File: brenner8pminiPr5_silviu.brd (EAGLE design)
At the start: 82.5 x 43 mm, 39 parts, among them IC1 PIC18F2550SP, Q1 20 MHz, Q2 BC338-25, Q3 BC338-25, Q4 BC328-25, Q5 BC328-25, Q6 BF959, X2 USB-B-H

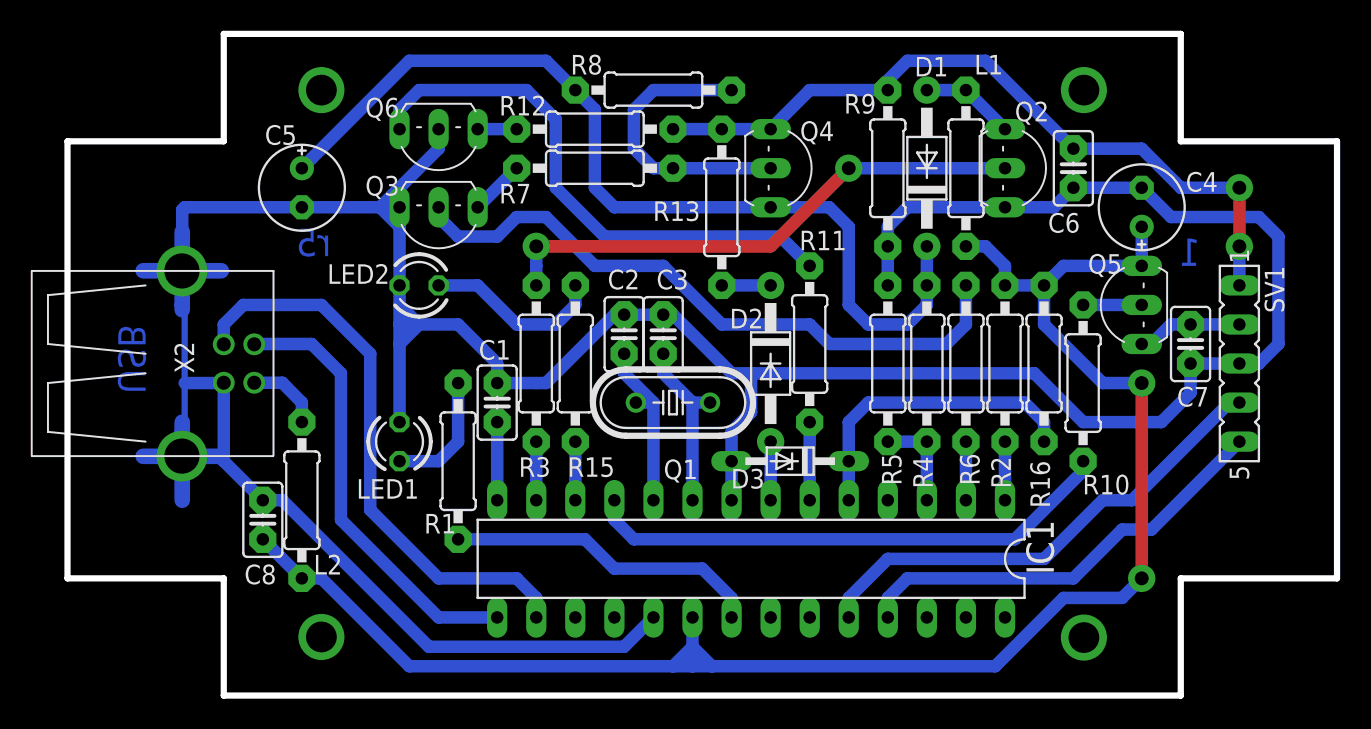
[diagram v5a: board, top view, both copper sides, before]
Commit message: Fixed D2-D3 overlap
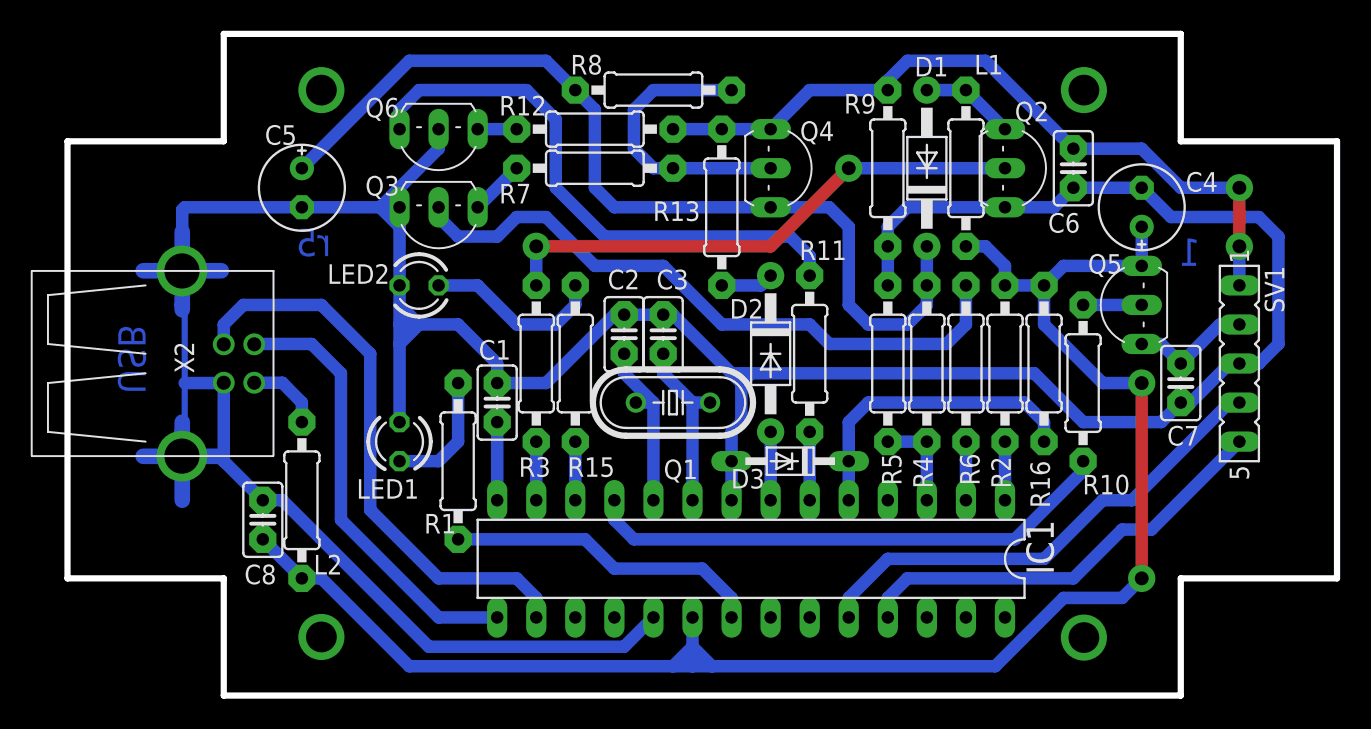
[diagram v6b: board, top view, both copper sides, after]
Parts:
- moved C7 2.62 mm to (72.4, 19.1)
- moved R11 0.64 mm to (48.3, 21.0)
- moved D2 0.63 mm to (45.7, 21.0)
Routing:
- net VSS: track 232.3 -> 231.0 mm
- net N$17: track 6.88 -> 7.93 mm
- net N$19: track 35.8 -> 36.8 mm
- net N$20: track 5.08 -> 4.45 mm
- net N$25: track 3.81 -> 4.45 mm
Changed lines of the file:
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@@
 <attribute name="VALUE" x="66.675" y="16.7894" size="1.27" layer="27" ratio="10" rot="R90"/>
 </element>
-<element name="C7" library="rcl" package="C025-025X050" value="100nF" x="73.025" y="21.59" smashed="yes" rot="R270">
-<attribute name="NAME" x="72.136" y="17.526" size="1.27" layer="25" ratio="10"/>
-<attribute name="VALUE" x="72.771" y="18.669" size="1.27" layer="27" ratio="10" rot="R270"/>
-</element>
-<element name="R11" library="rcl" package="0207/10" value="10k" x="48.26" y="21.59" smashed="yes" rot="R90">
-<attribute name="NAME" x="50.673" y="28.956" size="1.27" layer="25" ratio="10" rot="R180"/>
-<attribute name="VALUE" x="48.895" y="19.3294" size="1.27" layer="27" ratio="10" rot="R90"/>
+<element name="C7" library="rcl" package="C025-025X050" value="100nF" x="72.39" y="19.05" smashed="yes" rot="R270">
+<attribute name="NAME" x="71.501" y="14.986" size="1.27" layer="25" ratio="10"/>
+<attribute name="VALUE" x="72.136" y="16.129" size="1.27" layer="27" ratio="10" rot="R270"/>
+</element>
+<element name="R11" library="rcl" package="0207/10" value="10k" x="48.26" y="20.955" smashed="yes" rot="R90">
+<attribute name="NAME" x="50.673" y="28.321" size="1.27" layer="25" ratio="10" rot="R180"/>
+<attribute name="VALUE" x="48.895" y="18.6944" size="1.27" layer="27" ratio="10" rot="R90"/>
 </element>
 <element name="R12" library="rcl" package="0207/10" value="100" x="34.29" y="35.56" smashed="yes">
@@
 <attribute name="VALUE" x="43.18" y="29.4894" size="1.27" layer="27" ratio="10" rot="R90"/>
 </element>
-<element name="D2" library="diode" package="DO41-10" value="BAT43" x="45.72" y="20.32" smashed="yes" rot="R270">
-<attribute name="NAME" x="43.053" y="22.606" size="1.27" layer="25" ratio="10"/>
-<attribute name="VALUE" x="42.291" y="24.892" size="1.27" layer="27" ratio="10" rot="R270"/>
+<element name="D2" library="diode" package="DO41-10" value="BAT43" x="45.72" y="20.955" smashed="yes" rot="R270">
+<attribute name="NAME" x="43.053" y="23.241" size="1.27" layer="25" ratio="10"/>
+<attribute name="VALUE" x="42.291" y="25.527" size="1.27" layer="27" ratio="10" rot="R270"/>
 </element>
 <element name="Q6" library="sprut" package="TO92-BEC" value="BF959" x="24.13" y="35.56" smashed="yes" rot="R180">
@@
 <wire x1="30.48" y1="27.94" x2="45.72" y2="27.94" width="0.8128" layer="1"/>
 <wire x1="45.72" y1="27.94" x2="50.8" y2="33.02" width="0.8128" layer="1"/>
-<wire x1="30.48" y1="26.67" x2="30.48" y2="27.94" width="0.8128" layer="16"/>
-<wire x1="30.48" y1="26.67" x2="30.48" y2="25.4" width="0.8128" layer="16"/>
+<wire x1="30.48" y1="27.94" x2="30.48" y2="25.4" width="0.8128" layer="16"/>
 <via x="50.8" y="33.02" extent="1-16" drill="0.9" diameter="1.778"/>
 <via x="30.48" y="27.94" extent="1-16" drill="0.9" diameter="1.778"/>
@@
 <wire x1="34.29" y1="36.83" x2="34.29" y2="31.75" width="0.8128" layer="16"/>
 <wire x1="34.29" y1="31.75" x2="35.56" y2="30.48" width="0.8128" layer="16"/>
-<wire x1="15.24" y1="33.02" x2="15.875" y2="33.655" width="0.8128" layer="16"/>
-<wire x1="15.875" y1="33.655" x2="22.225" y2="40.005" width="0.8128" layer="16"/>
+<wire x1="15.24" y1="33.02" x2="22.225" y2="40.005" width="0.8128" layer="16"/>
 <wire x1="22.225" y1="40.005" x2="31.115" y2="40.005" width="0.8128" layer="16"/>
 <wire x1="31.115" y1="40.005" x2="33.02" y2="38.1" width="0.8128" layer="16"/>
@@
 <contactref element="R1" pad="1"/>
 <contactref element="IC1" pad="21"/>
-<wire x1="25.4" y1="8.89" x2="26.035" y2="8.89" width="0.8128" layer="16"/>
-<wire x1="26.035" y1="8.89" x2="33.655" y2="8.89" width="0.8128" layer="16"/>
+<wire x1="25.4" y1="8.89" x2="33.655" y2="8.89" width="0.8128" layer="16"/>
 <wire x1="33.655" y1="8.89" x2="35.56" y2="6.985" width="0.8128" layer="16"/>
 <wire x1="35.56" y1="6.985" x2="41.275" y2="6.985" width="0.8128" layer="16"/>
@@
 <contactref element="Q5" pad="C"/>
 <contactref element="C7" pad="1"/>
-<wire x1="69.85" y1="21.59" x2="70.485" y2="21.59" width="0.8128" layer="16"/>
-<wire x1="70.485" y1="21.59" x2="71.755" y2="22.86" width="0.8128" layer="16"/>
-<wire x1="71.755" y1="22.86" x2="73.025" y2="22.86" width="0.8128" layer="16"/>
-<wire x1="73.025" y1="22.86" x2="76.2" y2="22.86" width="0.8128" layer="16"/>
+<wire x1="69.85" y1="21.59" x2="71.12" y2="21.59" width="0.8128" layer="16"/>
+<wire x1="71.12" y1="21.59" x2="72.39" y2="20.32" width="0.8128" layer="16"/>
+<wire x1="72.39" y1="20.32" x2="74.93" y2="22.86" width="0.8128" layer="16"/>
+<wire x1="74.93" y1="22.86" x2="76.2" y2="22.86" width="0.8128" layer="16"/>
 </signal>
 <signal name="N$19">
 <contactref element="R11" pad="2"/>
 <contactref element="Q6" pad="B"/>
-<wire x1="46.355" y1="28.575" x2="48.26" y2="26.67" width="0.8128" layer="16"/>
-<wire x1="34.925" y1="28.575" x2="46.355" y2="28.575" width="0.8128" layer="16"/>
+<wire x1="46.99" y1="28.575" x2="48.26" y2="27.305" width="0.8128" layer="16"/>
+<wire x1="48.26" y1="27.305" x2="48.26" y2="26.035" width="0.8128" layer="16"/>
+<wire x1="34.925" y1="28.575" x2="46.99" y2="28.575" width="0.8128" layer="16"/>
 <wire x1="31.75" y1="31.75" x2="34.925" y2="28.575" width="0.8128" layer="16"/>
 <wire x1="31.75" y1="36.195" x2="31.75" y2="31.75" width="0.8128" layer="16"/>
@@
 <contactref element="R11" pad="1"/>
 <contactref element="IC1" pad="6"/>
-<wire x1="48.26" y1="11.43" x2="48.26" y2="16.51" width="0.8128" layer="16"/>
+<wire x1="48.26" y1="11.43" x2="48.26" y2="15.875" width="0.8128" layer="16"/>
 </signal>
 <signal name="N$22">
@@
 <contactref element="IC1" pad="7"/>
 <contactref element="D2" pad="A"/>
-<wire x1="45.72" y1="11.43" x2="45.72" y2="15.24" width="0.8128" layer="16"/>
+<wire x1="45.72" y1="11.43" x2="45.72" y2="15.875" width="0.8128" layer="16"/>
 </signal>
 <signal name="N$26">
 <contactref element="D2" pad="C"/>
 <contactref element="R13" pad="1"/>
-<wire x1="42.545" y1="25.4" x2="45.72" y2="25.4" width="0.8128" layer="16"/>
+<wire x1="42.545" y1="25.4" x2="45.085" y2="25.4" width="0.8128" layer="16"/>
+<wire x1="45.085" y1="25.4" x2="45.72" y2="26.035" width="0.8128" layer="16"/>
 </signal>
 <signal name="VDD">
@@
 <wire x1="66.04" y1="16.51" x2="71.12" y2="16.51" width="0.8128" layer="16"/>
 <wire x1="43.18" y1="13.97" x2="43.18" y2="11.43" width="0.8128" layer="16"/>
-<wire x1="44.45" y1="17.145" x2="43.18" y2="15.875" width="0.8128" layer="16"/>
+<wire x1="43.815" y1="16.51" x2="43.18" y2="15.875" width="0.8128" layer="16"/>
 <wire x1="43.18" y1="15.875" x2="43.18" y2="13.97" width="0.8128" layer="16"/>
 <wire x1="77.47" y1="29.845" x2="71.755" y2="29.845" width="0.8128" layer="16"/>
-<wire x1="27.94" y1="19.05" x2="30.48" y2="19.05" width="0.8128" layer="16"/>
-<wire x1="30.48" y1="19.05" x2="31.115" y2="19.05" width="0.8128" layer="16"/>
+<wire x1="27.94" y1="19.05" x2="31.115" y2="19.05" width="0.8128" layer="16"/>
 <wire x1="10.16" y1="19.05" x2="10.16" y2="19.07" width="0.8128" layer="16"/>
 <wire x1="10.16" y1="13.97" x2="12.7" y2="11.43" width="0.8128" layer="16"/>
@@
 <wire x1="7.4612" y1="11.43" x2="7.4612" y2="15.875" width="1.016" layer="16"/>
 <wire x1="7.4612" y1="15.875" x2="7.4612" y2="16.51" width="1.016" layer="16"/>
-<wire x1="43.18" y1="19.685" x2="44.45" y2="19.685" width="0.8128" layer="16"/>
+<wire x1="43.18" y1="19.685" x2="43.815" y2="19.685" width="0.8128" layer="16"/>
+<wire x1="43.815" y1="19.685" x2="44.45" y2="19.685" width="0.8128" layer="16"/>
 <wire x1="44.45" y1="19.685" x2="62.865" y2="19.685" width="0.8128" layer="16"/>
 <wire x1="36.195" y1="1.905" x2="38.1" y2="3.81" width="0.8128" layer="16"/>
@@
 <wire x1="21.59" y1="22.86" x2="22.86" y2="22.86" width="0.8128" layer="16"/>
 <wire x1="22.86" y1="22.86" x2="25.4" y2="22.86" width="0.8128" layer="16"/>
-<wire x1="71.12" y1="16.51" x2="73.025" y2="18.415" width="0.8128" layer="16"/>
-<wire x1="73.025" y1="18.415" x2="73.025" y2="20.32" width="0.8128" layer="16"/>
-<wire x1="73.025" y1="20.32" x2="76.2" y2="20.32" width="0.8128" layer="16"/>
+<wire x1="71.12" y1="16.51" x2="72.39" y2="17.78" width="0.8128" layer="16"/>
 <wire x1="36.195" y1="23.495" x2="38.735" y2="23.495" width="0.8128" layer="16"/>
 <wire x1="35.56" y1="23.495" x2="36.195" y2="23.495" width="0.8128" layer="16"/>
@@
 <wire x1="21.59" y1="30.48" x2="21.59" y2="31.75" width="0.8128" layer="16"/>
 <wire x1="24.13" y1="34.29" x2="24.13" y2="35.56" width="0.8128" layer="16"/>
-<wire x1="44.45" y1="17.145" x2="44.45" y2="19.685" width="0.8128" layer="16"/>
+<wire x1="43.815" y1="16.51" x2="43.815" y2="19.05" width="0.8128" layer="16"/>
+<wire x1="43.815" y1="19.05" x2="43.815" y2="19.685" width="0.8128" layer="16"/>
 <wire x1="21.59" y1="21.59" x2="22.86" y2="22.86" width="0.8128" layer="16"/>
 <wire x1="22.86" y1="22.86" x2="21.59" y2="24.13" width="0.8128" layer="16"/>
-<wire x1="20.32" y1="30.48" x2="21.59" y2="31.75" width="0.8128" layer="16"/>
 <wire x1="21.59" y1="31.75" x2="20.32" y2="30.48" width="0.8128" layer="16"/>
 <wire x1="21.59" y1="29.21" x2="20.32" y2="30.48" width="0.8128" layer="16"/>
+<wire x1="72.39" y1="17.78" x2="73.025" y2="17.78" width="0.8128" layer="16"/>
+<wire x1="73.025" y1="17.78" x2="75.565" y2="20.32" width="0.8128" layer="16"/>
+<wire x1="75.565" y1="20.32" x2="76.2" y2="20.32" width="0.8128" layer="16"/>
+<wire x1="43.18" y1="19.685" x2="43.815" y2="19.05" width="0.8128" layer="16"/>
+<wire x1="43.815" y1="19.05" x2="44.45" y2="19.685" width="0.8128" layer="16"/>
 </signal>
 <signal name="N$29">

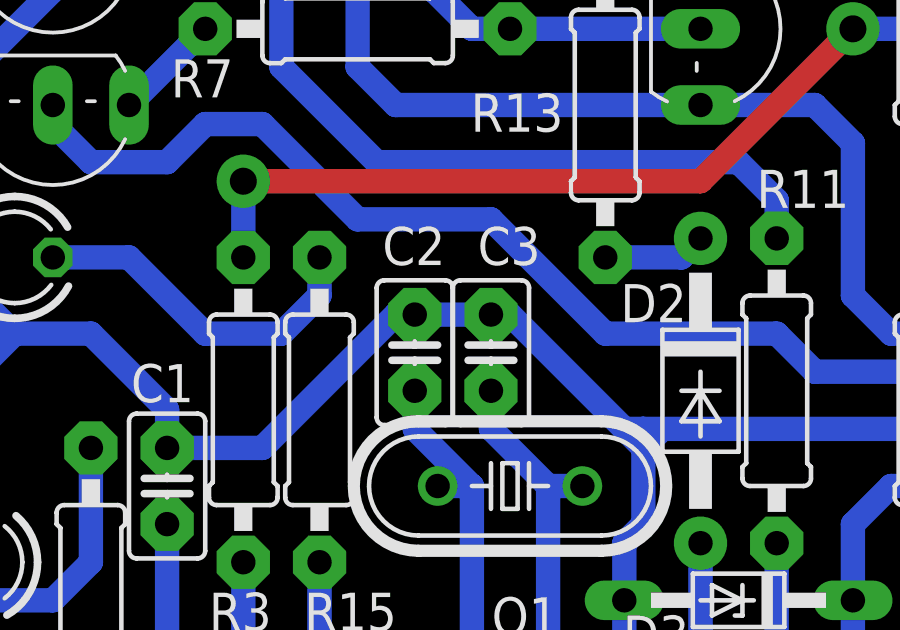
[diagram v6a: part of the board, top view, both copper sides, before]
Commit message: Removed layer 116
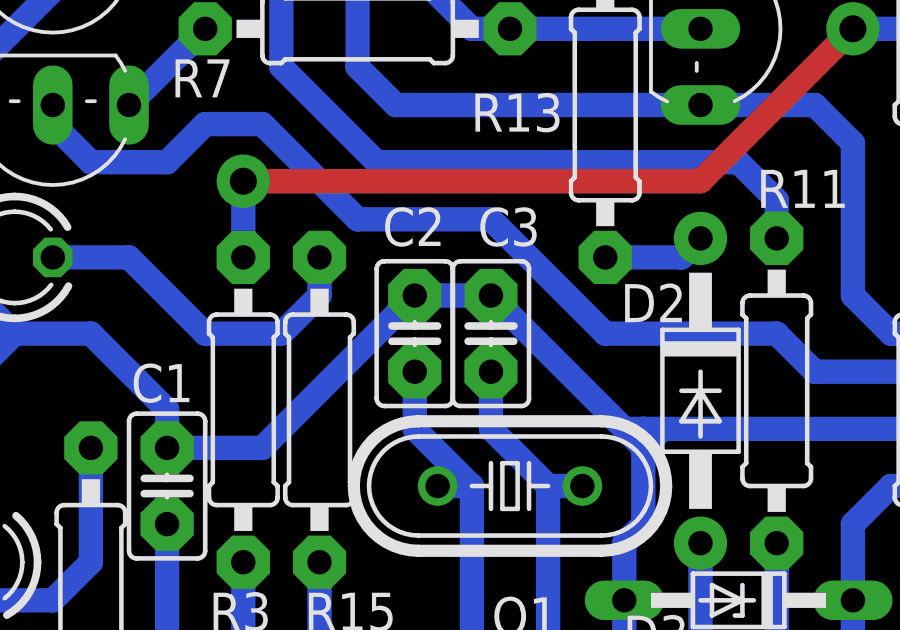
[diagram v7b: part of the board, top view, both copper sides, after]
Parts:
- moved C2 0.63 mm to (36.2, 22.9)
- moved C3 0.63 mm to (38.7, 22.9)
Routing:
- net N$7: track 11.5 -> 12.1 mm
- net N$6: track 11.5 -> 12.1 mm
- net VSS: track 231.0 -> 231.5 mm
